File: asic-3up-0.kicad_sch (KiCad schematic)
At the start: 63 parts, among them J3 Conn_01x01, J4 Conn_01x01, U28 MCP1824T-1202E/OT, U29 MCP1824T-1202E/OT, U30 MCP1824T-1202E/OT, U32 MCP1824T-0802E, U42 MCP1824T-0802E, U43 MCP1824T-0802E, U45 BM1362AC_MODE1, U46 BM1362AC_MODE0, U47 BM1362AC_MODE1

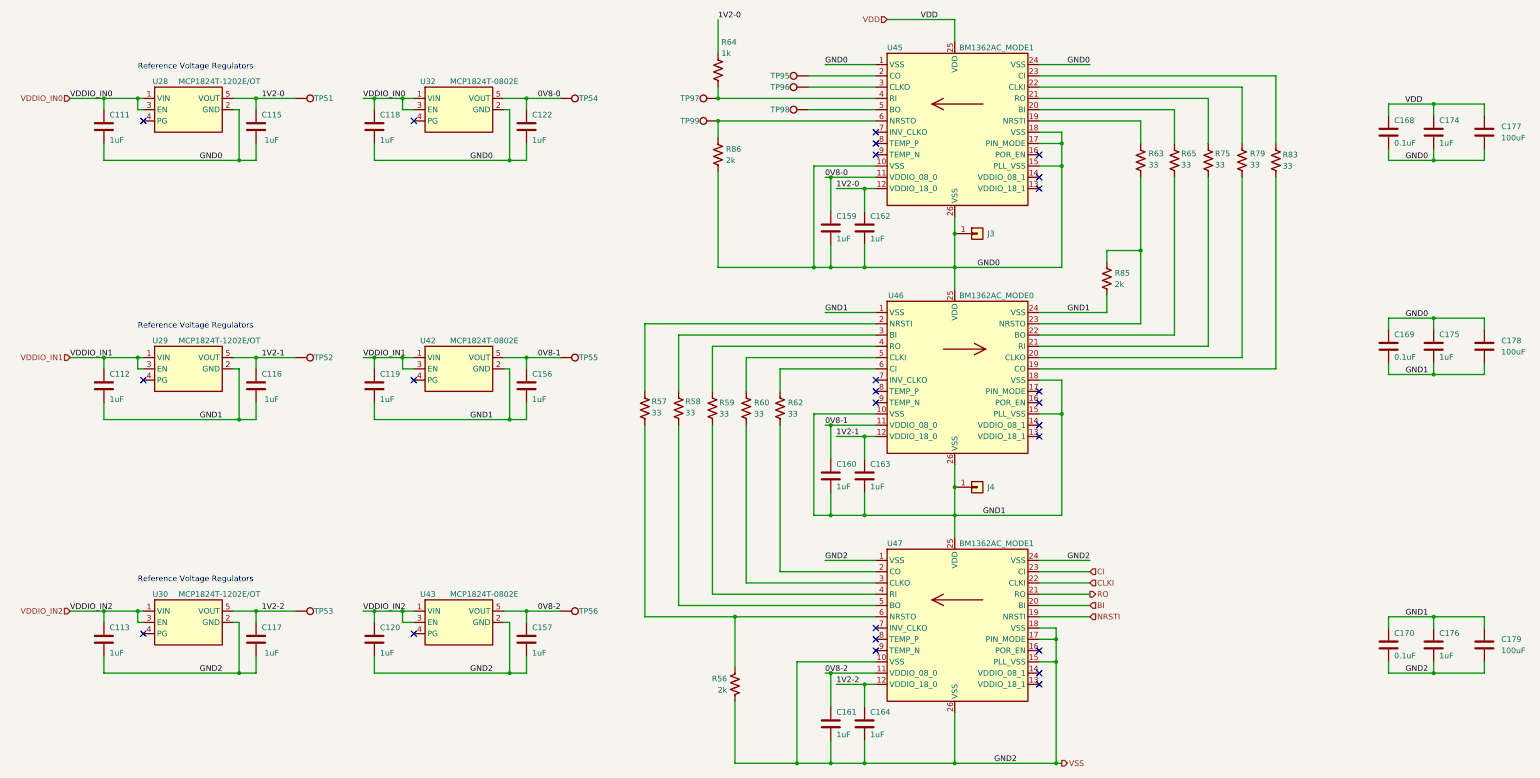
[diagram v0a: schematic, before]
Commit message: added topside data test pads. cleaned up power pads some more.
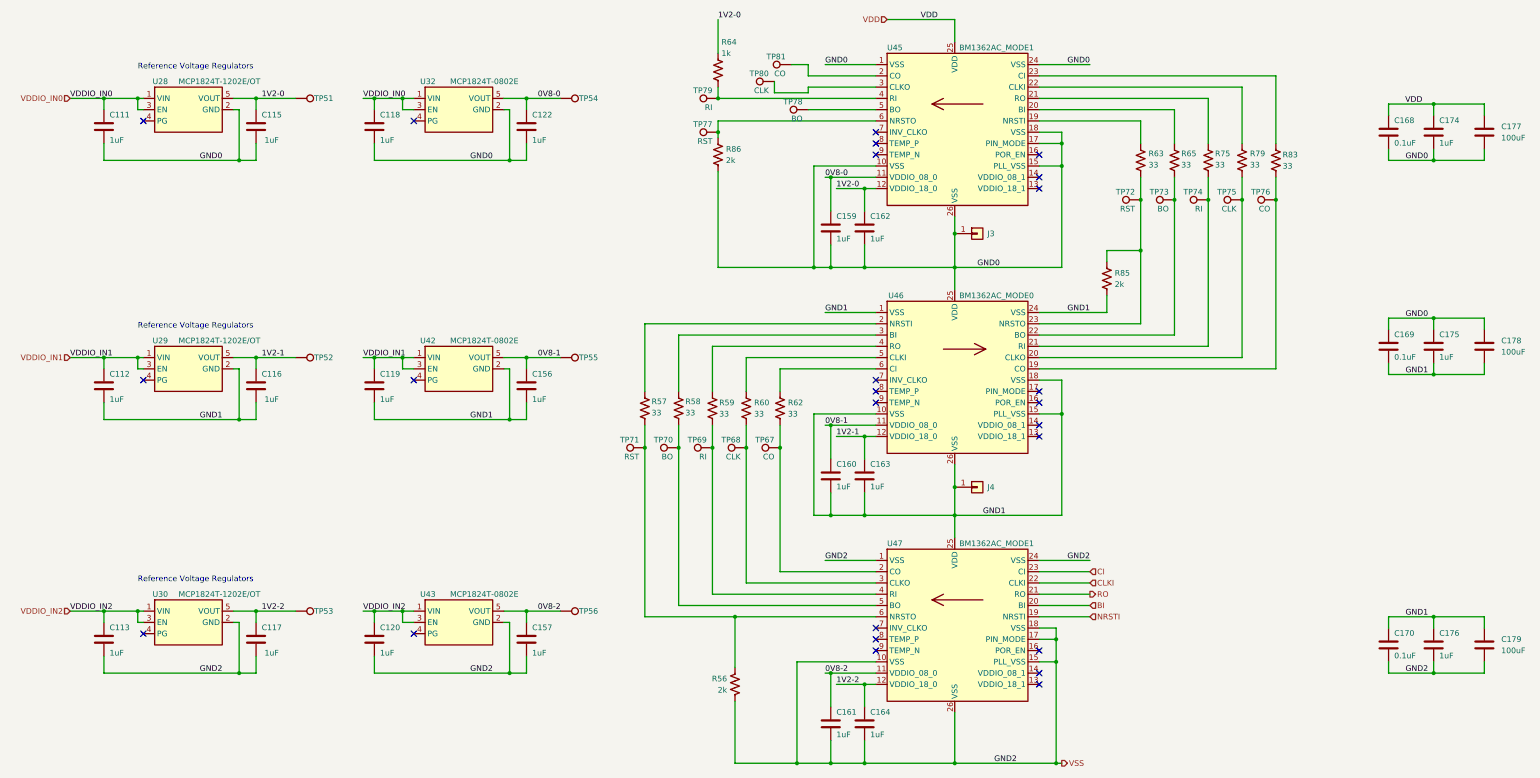
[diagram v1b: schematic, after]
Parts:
- removed TP95, TP96, TP97, TP98, TP99: TestPoint, TestPoint:TestPoint_Pad_D1.0mm, symbol Connector:TestPoint
- added TP67, TP76, TP81: CO, emberone:TestPoint_Pad_1.0x0.4mm, symbol Connector:TestPoint
- added TP68, TP75, TP80: CLK, emberone:TestPoint_Pad_1.0x0.4mm, symbol Connector:TestPoint
- added TP69, TP74, TP79: RI, emberone:TestPoint_Pad_1.0x0.4mm, symbol Connector:TestPoint
- added TP70, TP73, TP78: BO, emberone:TestPoint_Pad_1.0x0.4mm, symbol Connector:TestPoint
- added TP71, TP72, TP77: RST, emberone:TestPoint_Pad_1.0x0.4mm, symbol Connector:TestPoint
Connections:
- net at R65.2, U46.22 (BO): now also TP73.1
- net at R83.2, U46.19 (CO): now also TP76.1
- net at R86.1, U45.6 (NRSTO): now also TP77.1
- net at U45.2 (CO): now also TP81.1
- net at R62.2, U47.2 (CO): now also TP67.1
- net at U45.3 (CLKO): now also TP80.1
- net at R64.2, U45.4 (RI): now also TP79.1
- net at U45.5 (BO): now also TP78.1
- net at R63.2, R85.1, U46.23 (NRSTO): now also TP72.1
- net at R79.2, U46.20 (CLKO): now also TP75.1
- net at R75.2, U46.21 (RI): now also TP74.1
- net at R60.2, U47.3 (CLKO): now also TP68.1
- net at R59.2, U47.4 (RI): now also TP69.1
- net at R58.2, U47.5 (BO): now also TP70.1
- net at R56.1, R57.2, U47.6 (NRSTO): now also TP71.1

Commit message: add BOM, iBOM and position files
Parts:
- J3, J4: now left out of the parts list
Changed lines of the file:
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@@
 		(unit 1)
 		(exclude_from_sim no)
-		(in_bom yes)
+		(in_bom no)
 		(on_board yes)
 		(dnp no)
@@
 		(unit 1)
 		(exclude_from_sim no)
-		(in_bom yes)
-		(on_board yes)
-		(dnp no)
+		(in_bom no)
+		(on_board yes)
+		(dnp no)

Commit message: corrected the voltage regulator input and output capacitors. Updated BOM, iBOM, cpos, gerbers and render.
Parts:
- U45, U46, U47: PARTNO (none) -> BM1362AC
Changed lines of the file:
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@@
+			)
+		)
+		(property "PARTNO" "BM1362AC"
+			(at 248.92 78.74 0)
+			(effects
+				(font
+					(size 1.27 1.27)
+				)
+				(hide yes)
 			)
 		)
@@
 			)
 		)
+		(property "PARTNO" "BM1362AC"
+			(at 248.92 134.62 0)
+			(effects
+				(font
+					(size 1.27 1.27)
+				)
+				(hide yes)
+			)
+		)
 		(pin "10"
 		)
@@
 			(at 248.92 190.5 0)
 			(effects
+				(font
+					(size 1.27 1.27)
+				)
+				(hide yes)
+			)
+		)
+		(property "PARTNO" "BM1362AC"
+			(at 248.92 190.5 0)
+			(effects

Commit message: bump version to v6
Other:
- company: (none) -> 256Foundation
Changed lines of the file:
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@@
 	(title_block
 		(title "emberOne/00")
-		(date "2025-09-17")
-		(rev "5")
+		(date "2026-02-17")
+		(rev "v6")
+		(company "256Foundation")
+		(comment 1 "OHL-S-2.0")
 	)
 	(text "Reference Voltage Regulators"
